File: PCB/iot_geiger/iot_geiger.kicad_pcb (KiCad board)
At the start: 2 copper layers, 99.1 x 63.5 mm, 59 parts, among them J1 Program, J2 Display, J3 IO, J4 5V DC, J5 PM, Q1 BUK7M6R3, Q2 BC817, SW1 SW_Update, U1 NINA-W102, U2 AM2302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

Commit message: fix spiffs
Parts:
- added R19: 10K, Resistor_SMD:R_0603_1608Metric_Pad0.98x0.95mm_HandSolder, F.Cu at (138.7, 79.5)
- added V1: J305, nina:Geiger, F.Cu at (118.1, 44.5)
- moved R8 0.92 mm to (197.4, 68.3)
- moved R4 0.25 mm to (192.8, 81.8)
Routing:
- net +3V3: track 214.1 -> 201.4 mm
- net Net-(C7-Pad2): track 3.57 -> 14.9 mm
- net Net-(R14-Pad2): track 0.00 -> 7.20 mm
- net +5V: track 102.5 -> 104.4 mm
- net Net-(Q1-Pad4): track 2.04 -> 3.82 mm
- net /PM_TxD: track 89.4 -> 87.9 mm
- net GND: track 88.7 -> 90.2 mm, vias 43 -> 45
- net /G_ANA: track 55.9 -> 54.4 mm
- net /PRG_RxD: track 113.8 -> 112.7 mm
- net Net-(R8-Pad1): track 5.69 -> 4.57 mm
- net /PM_RxD: track 85.5 -> 84.7 mm
- net /IO2: track 75.6 -> 74.8 mm
- net /PRG_TxD: track 107.2 -> 106.5 mm
- net /PM_RST: track 78.2 -> 77.6 mm
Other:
- board size 99.1 x 63.5 mm -> 99.1 x 64.5 mm

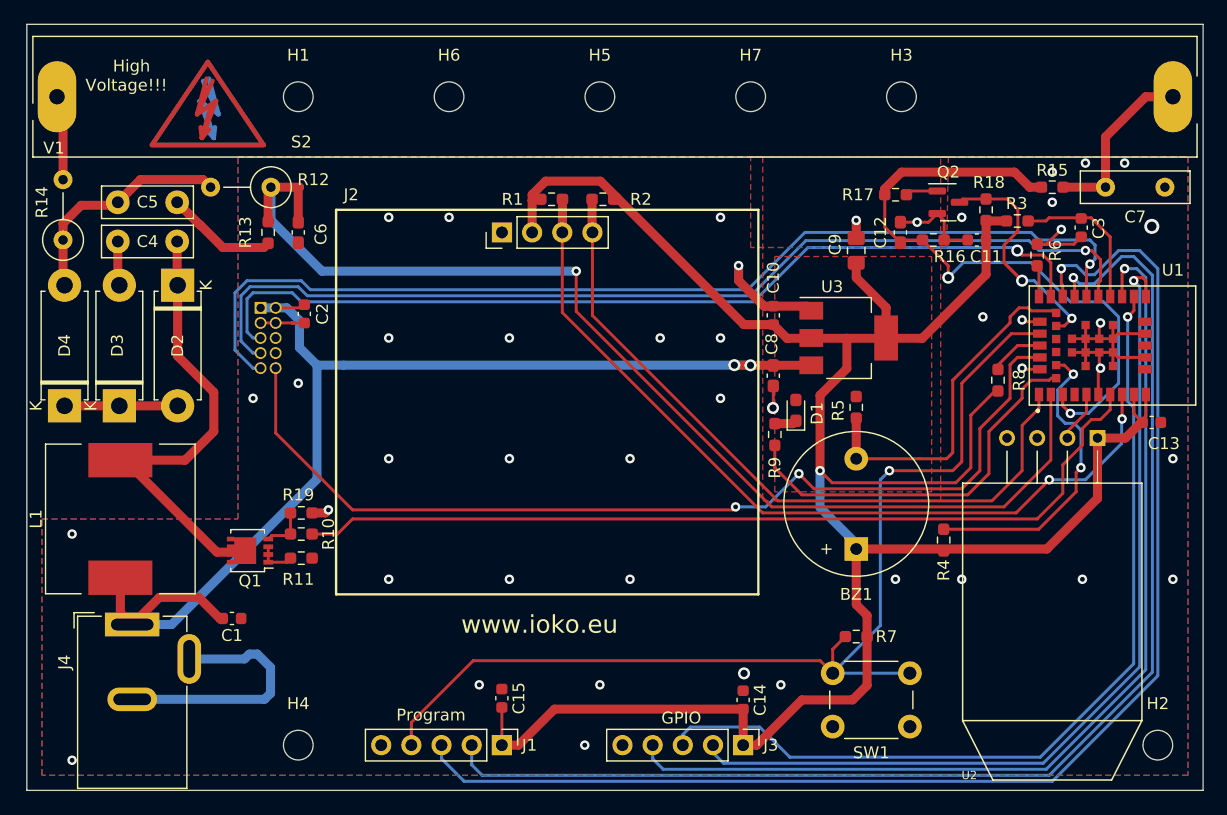
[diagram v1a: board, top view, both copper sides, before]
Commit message: Add PM sensor support
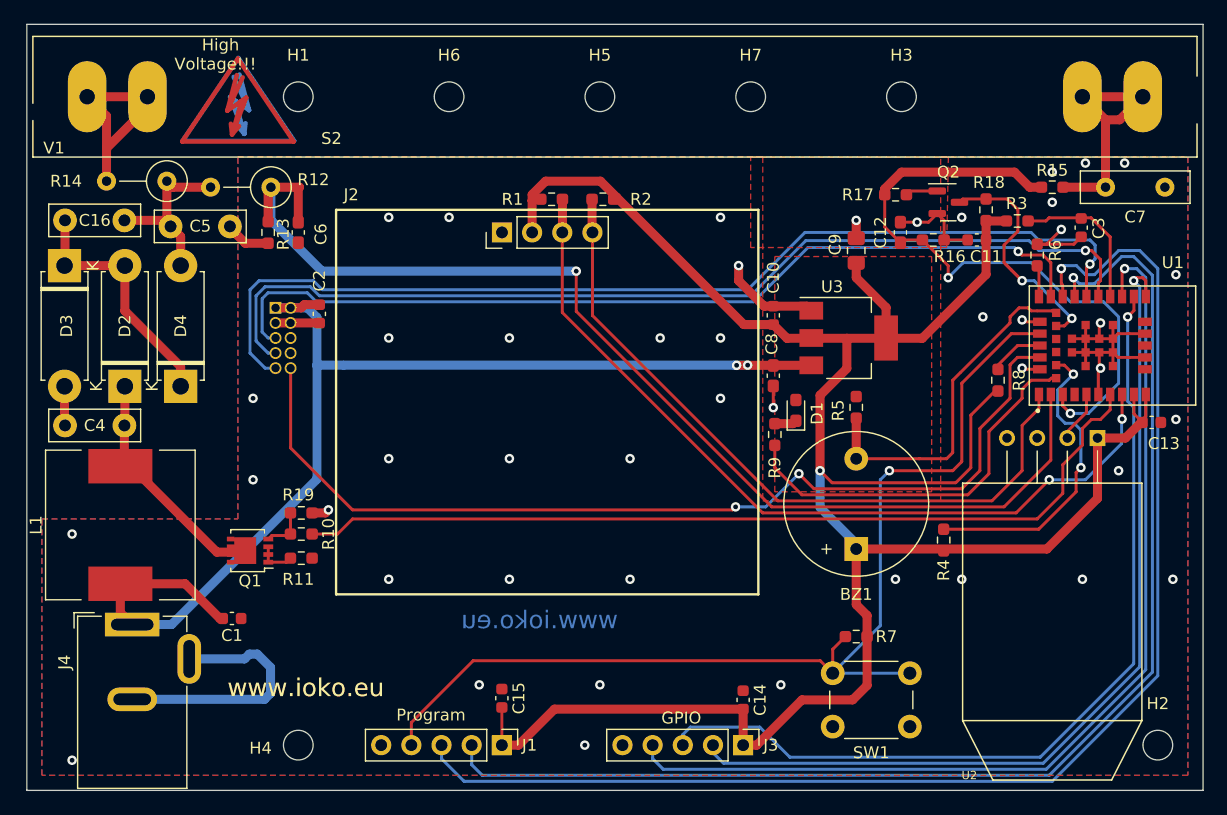
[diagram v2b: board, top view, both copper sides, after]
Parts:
- added C16: 10nF/1000v, Capacitor_THT:C_Disc_D7.5mm_W2.5mm_P5.00mm, F.Cu at (118.8, 54.9)
- C6: value 0.1nF -> 100pF
- R11: value 10R -> 47R
- moved C4 16.1 mm to (123.8, 72.1)
- moved D3 12.7 mm to (118.7, 58.7), turned to -90 degrees
- moved R14 10.0 mm to (127.4, 51.6), turned to 180 degrees
- moved D4 9.92 mm to (128.5, 68.8)
- moved D2 9.60 mm to (123.8, 68.8), turned to 90 degrees
- moved C5 4.89 mm to (132.7, 55.4)
- moved S1 2.60 mm to (133.4, 45.4)
- moved S2 2.56 mm to (133.3, 45.4)
- moved C2 1.27 mm to (140.2, 62.7)
- moved J5 1.26 mm to (136.5, 62.2)
- moved L1 0.51 mm to (123.4, 80.5)
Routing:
- net Net-(C4-Pad1): track 39.9 -> 20.7 mm
- net Net-(D2-Pad2): track 9.53 -> 21.0 mm
- net Net-(R14-Pad2): track 7.20 -> 18.6 mm
- net Net-(C7-Pad2): track 14.9 -> 21.0 mm
- net GND: track 90.2 -> 84.7 mm
- net Net-(D4-Pad2): track 19.4 -> 15.6 mm
- net /PM_RST: track 77.6 -> 76.4 mm
- net /PM_RxD: track 84.7 -> 83.4 mm
- net /PM_TxD: track 87.9 -> 86.9 mm
- net /PM_SET: track 82.6 -> 82.1 mm

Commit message: PCB updated
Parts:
- added R20: 22K, Resistor_SMD:R_0603_1608Metric_Pad0.98x0.95mm_HandSolder, F.Cu at (210.1, 73.7)
- C3: value 100nF -> DNU
- D2, D3, D4: footprint Diode_THT:D_5W_P10.16mm_Horizontal -> Diode_THT:D_DO-41_SOD81_P10.16mm_Horizontal
- Q1: value BUK7M6R3 -> BSS123; footprint Package_TO_SOT_SMD:LFPAK33 -> Package_TO_SOT_SMD:SOT-23
- R11: value 47R -> 10R
- R12: value 22M -> 47M
- R13: value 150K -> 330K
- R15: value 22K -> 10K
- R16: value 100K -> 220K
- R3: value 10K* -> DNU
- R4: value 47K -> DNU
- R5: value 10K -> DNU
- R6, R8: value 47K -> 10K
- moved D2 10.2 mm to (123.7, 58.7), turned to -90 degrees
- moved D3 10.2 mm to (118.9, 68.8), turned to 90 degrees
- moved D4 10.2 mm to (128.5, 58.7), turned to -90 degrees
- moved R11 7.27 mm to (135.6, 76.7), turned to -90 degrees
- moved Q1 2.17 mm to (134.6, 80.5)
- moved C2 1.03 mm to (140.5, 63.7)
- moved J5 0.78 mm to (136.5, 63.0)
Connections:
- C16 pad 1: Net-(D2-Pad2) -> Net-(C16-Pad1)
- C16 pad 2: Net-(D4-Pad2) -> Net-(C16-Pad2)
- C5 pad 2: Net-(D4-Pad2) -> Net-(C16-Pad2)
- D2 pad 1: Net-(C4-Pad1) -> Net-(C16-Pad1)
- D2 pad 2: Net-(D2-Pad2) -> Net-(C4-Pad1)
- D3 pad 1: Net-(D2-Pad2) -> Net-(C4-Pad2)
- D3 pad 2: Net-(C4-Pad2) -> Net-(C16-Pad1)
- D4 pad 1: Net-(D2-Pad2) -> Net-(C16-Pad2)
- D4 pad 2: Net-(D4-Pad2) -> Net-(C4-Pad2)
- Q1 pad 1: Net-(Q1-Pad1) -> Net-(R10-Pad1)
- Q1 pad 2: Net-(Q1-Pad1) -> Net-(R11-Pad2)
- Q1 pad 3: Net-(Q1-Pad1) -> Net-(C4-Pad1)
- R10 pad 1: Net-(Q1-Pad4) -> Net-(R10-Pad1)
- R11 pad 2: Net-(Q1-Pad1) -> Net-(R11-Pad2)
- R12 pad 2: Net-(D4-Pad2) -> Net-(C16-Pad2)
- R14 pad 1: Net-(D4-Pad2) -> Net-(C16-Pad2)
- R19 pad 2: Net-(Q1-Pad4) -> Net-(R10-Pad1)
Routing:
- net Net-(D2-Pad2): track 21.0 -> 0.00 mm
- net Net-(D4-Pad2): track 15.6 -> 0.00 mm
- net Net-(C16-Pad2): track 0.00 -> 15.6 mm
- net Net-(C4-Pad2): track 3.32 -> 17.3 mm
- net /TEMP_SEN: track 4.33 -> 16.8 mm, vias 0 -> 1
- net Net-(C16-Pad1): track 0.00 -> 8.80 mm
- net +5V: track 104.0 -> 108.4 mm
- net Net-(R10-Pad1): track 0.00 -> 4.25 mm
- net Net-(Q1-Pad4): track 3.82 -> 0.00 mm
- net Net-(Q1-Pad1): track 3.31 -> 0.00 mm
- net /SCL: track 70.2 -> 72.7 mm
- net Net-(R11-Pad2): track 0.00 -> 1.98 mm
- net +3V3: track 201.4 -> 202.7 mm
- net Net-(C4-Pad1): track 20.7 -> 19.5 mm
- net /PM_SET: track 82.1 -> 81.3 mm
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
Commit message: AP added
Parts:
- Q1: value BSS123 -> PBHV8540Z; footprint Package_TO_SOT_SMD:SOT-23 -> Package_TO_SOT_SMD:SOT-223
- R10: value 10R -> 2K2
- R11: value 10R -> 47R
- moved R19 7.89 mm to (138.2, 71.6), turned to -90 degrees
- moved R10 5.62 mm to (140.5, 75.9), turned to -90 degrees
- moved R11 5.47 mm to (133.6, 71.6)
- moved Q1 2.84 mm to (135.9, 78.0), turned to -90 degrees
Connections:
- Q1 pad 2: Net-(R11-Pad2) -> Net-(C4-Pad1)
- Q1 pad 3: Net-(C4-Pad1) -> Net-(R11-Pad2)
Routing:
- net Net-(C4-Pad1): track 19.5 -> 26.9 mm
- net GND: track 84.7 -> 83.3 mm
- net /PM_SET: track 81.3 -> 80.6 mm

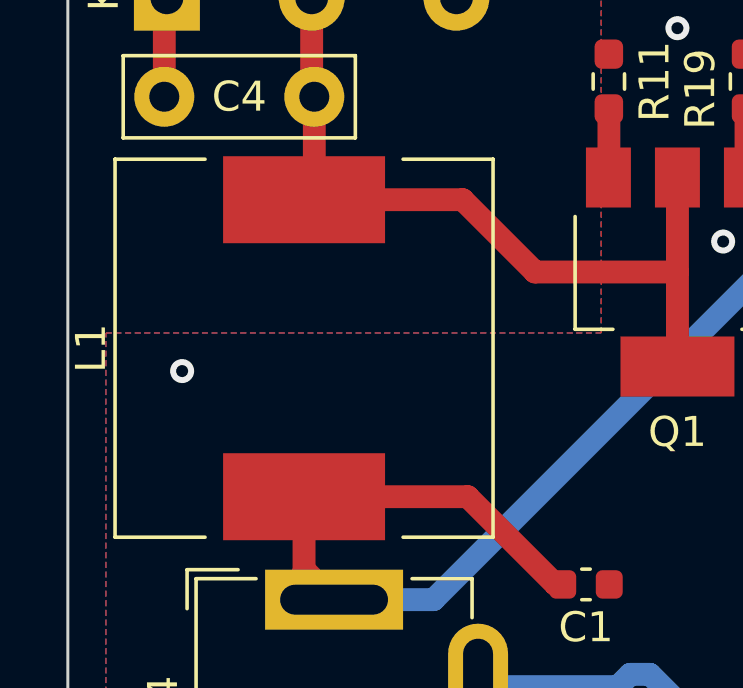
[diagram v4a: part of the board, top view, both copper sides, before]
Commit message: add webserver
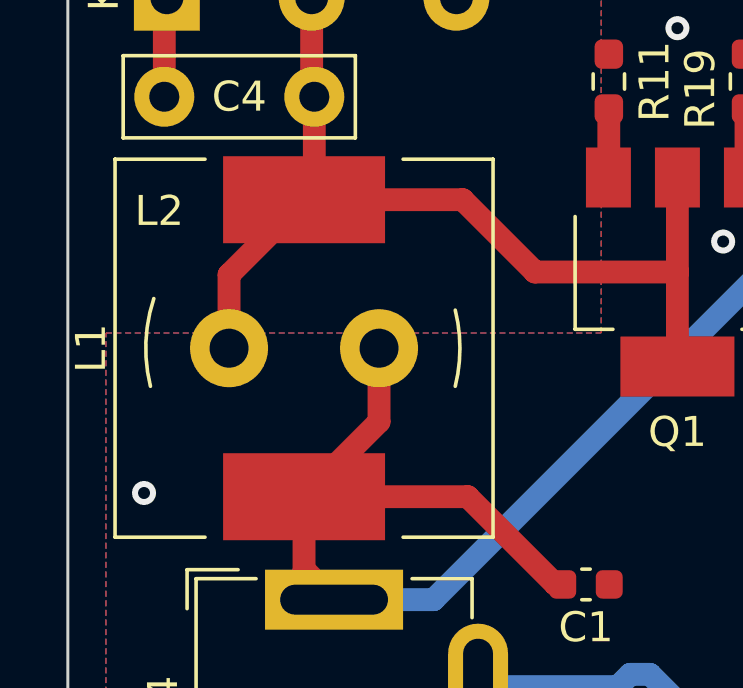
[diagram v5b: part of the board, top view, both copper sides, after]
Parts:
- added L2: DNU, Inductor_THT:L_Radial_D10.0mm_P5.00mm_Fastron_07M, F.Cu at (125.9, 80.5)
- Q1: value PBHV8540Z -> PZTA42
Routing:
- net Net-(C4-Pad1): track 26.9 -> 32.9 mm
- net +5V: track 108.4 -> 114.4 mm
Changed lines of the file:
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@@
   (net 37 "Net-(C16-Pad2)")
   (net 38 "unconnected-(U1-Pad4)")
-  (net 39 "Net-(R10-Pad1)")
-  (net 40 "Net-(R11-Pad2)")
+  (net 39 "Net-(Q1-Pad1)")
+  (net 40 "Net-(Q1-Pad3)")
   (net 41 "Net-(C4-Pad2)")
   (net 42 "Net-(C16-Pad1)")
@@
       (effects (font (size 1 1) (thickness 0.15)))
     )
-    (fp_text value "PBHV8540Z" (at 0 4.5 90) (layer "F.Fab")
+    (fp_text value "PZTA42" (at 0 4.5 90) (layer "F.Fab")
       (effects (font (size 1 1) (thickness 0.15)))
     )
@@
     (fp_line (start -1.85 -2.3) (end -1.85 3.35) (layer "F.Fab") (width 0.1))
     (pad "1" smd rect (at -3.15 -2.3 270) (size 2 1.5) (layers "F.Cu" "F.Paste" "F.Mask")
-      (net 39 "Net-(R10-Pad1)") (pinfunction "B") (pintype "input"))
+      (net 39 "Net-(Q1-Pad1)") (pinfunction "B") (pintype "input"))
     (pad "2" smd rect (at -3.15 0 270) (size 2 1.5) (layers "F.Cu" "F.Paste" "F.Mask")
       (net 32 "Net-(C4-Pad1)") (pinfunction "C") (pintype "passive"))
     (pad "3" smd rect (at -3.15 2.3 270) (size 2 1.5) (layers "F.Cu" "F.Paste" "F.Mask")
-      (net 40 "Net-(R11-Pad2)") (pinfunction "E") (pintype "passive"))
+      (net 40 "Net-(Q1-Pad3)") (pinfunction "E") (pintype "passive"))
     (pad "4" smd rect (at 3.15 0 270) (size 2 3.8) (layers "F.Cu" "F.Paste" "F.Mask")
       (net 32 "Net-(C4-Pad1)") (pinfunction "C") (pintype "passive"))
@@
       (net 6 "GND") (pintype "passive"))
     (pad "2" smd roundrect (at 0.9125 0 270) (size 0.975 0.95) (layers "F.Cu" "F.Paste" "F.Mask") (roundrect_rratio 0.25)
-      (net 39 "Net-(R10-Pad1)") (pintype "passive"))
+      (net 39 "Net-(Q1-Pad1)") (pintype "passive"))
     (model "${KICAD6_3DMODEL_DIR}/Resistor_SMD.3dshapes/R_0603_1608Metric.wrl"
       (offset (xyz 0 0 0))
@@
     )
   )
+  (footprint "Inductor_THT:L_Radial_D10.0mm_P5.00mm_Fastron_07M" (layer "F.Cu")
+    (at 125.944 80.518 180)
+    (descr "Inductor, Radial series, Radial, pin pitch=5.00mm, , diameter=10mm, Fastron, 07M, http://www.fastrongroup.com/image-show/37/07M.pdf?type=Complete-DataSheet&productType=series")
+    (tags "Inductor Radial series Radial pin pitch 5.00mm  diameter 10mm Fastron 07M")
+    (property "Sheetfile" "iot_geiger.kicad_sch")
+    (property "Sheetname" "")
+    (attr through_hole)
+    (fp_text reference "L2" (at 7.326 4.572) (layer "F.SilkS")
+      (effects (font (size 1 1) (thickness 0.15)))
+    )
+    (fp_text value "DNU" (at 2.5 6.25) (layer "F.Fab")
+      (effects (font (size 1 1) (thickness 0.15)))
+    )
+    (fp_text user "${REFERENCE}" (at 2.5 0) (layer "F.Fab")
+      (effects (font (size 1 1) (thickness 0.15)))
+    )
+    (fp_arc (start 7.62 -1.27) (mid 7.772487 0.200953) (end 7.507632 1.655877) (layer "F.SilkS") (width 0.12))
+    (fp_arc (start -2.54 1.27) (mid -2.696344 0) (end -2.54 -1.27) (layer "F.SilkS") (width 0.12))
+    (fp_circle (center 2.5 0) (end 7.75 0) (layer "F.CrtYd") (width 0.05) (fill none))
+    (fp_circle (center 2.5 0) (end 7.5 0) (layer "F.Fab") (width 0.1) (fill none))
+    (pad "1" thru_hole circle (at 0 0 180) (size 2.6 2.6) (drill 1.3) (layers *.Cu *.Mask)
+      (net 18 "+5V") (pinfunction "1") (pintype "input"))
+    (pad "2" thru_hole circle (at 5 0 180) (size 2.6 2.6) (drill 1.3) (layers *.Cu *.Mask)
+      (net 32 "Net-(C4-Pad1)") (pinfunction "2") (pintype "input"))
+    (model "${KICAD6_3DMODEL_DIR}/Inductor_THT.3dshapes/L_Radial_D10.0mm_P5.00mm_Fastron_07M.wrl"
+      (offset (xyz 0 0 0))
+      (scale (xyz 1 1 1))
+      (rotate (xyz 0 0 0))
+    )
+  )
   (footprint "Resistor_SMD:R_0603_1608Metric_Pad0.98x0.95mm_HandSolder" (layer "F.Cu")
     (at 140.462 75.946 -90)
@@
     (fp_line (start -0.8 0.4125) (end -0.8 -0.4125) (layer "F.Fab") (width 0.1))
     (pad "1" smd roundrect (at -0.9125 0 270) (size 0.975 0.95) (layers "F.Cu" "F.Paste" "F.Mask") (roundrect_rratio 0.25)
-      (net 39 "Net-(R10-Pad1)") (pintype "passive"))
+      (net 39 "Net-(Q1-Pad1)") (pintype "passive"))
     (pad "2" smd roundrect (at 0.9125 0 270) (size 0.975 0.95) (layers "F.Cu" "F.Paste" "F.Mask") (roundrect_rratio 0.25)
       (net 22 "/PWM") (pintype "passive"))
@@
       (net 6 "GND") (pintype "passive"))
     (pad "2" smd roundrect (at 0.9125 0 270) (size 0.975 0.95) (layers "F.Cu" "F.Paste" "F.Mask") (roundrect_rratio 0.25)
-      (net 40 "Net-(R11-Pad2)") (pintype "passive"))
+      (net 40 "Net-(Q1-Pad3)") (pintype "passive"))
     (model "${KICAD6_3DMODEL_DIR}/Resistor_SMD.3dshapes/R_0603_1608Metric.wrl"
       (offset (xyz 0 0 0))
@@
   (via (at 201.93 50.8) (size 0.8) (drill 0.4) (layers "F.Cu" "B.Cu") (free) (net 6))
   (via (at 146.05 85.09) (size 0.8) (drill 0.4) (layers "F.Cu" "B.Cu") (free) (net 6))
-  (via (at 119.38 81.28) (size 0.8) (drill 0.4) (layers "F.Cu" "B.Cu") (free) (net 6))
+  (via (at 118.11 85.344) (size 0.8) (drill 0.4) (layers "F.Cu" "B.Cu") (free) (net 6))
   (via (at 166.37 74.93) (size 0.8) (drill 0.4) (layers "F.Cu" "B.Cu") (free) (net 6))
   (via (at 212.344 59.436) (size 0.8) (drill 0.4) (layers "F.Cu" "B.Cu") (free) (net 6))
@@
   (segment (start 181.635 67.07) (end 175.3476 67.07) (width 0.762) (layer "F.Cu") (net 18))
   (segment (start 128.902 85.468) (end 123.444 85.468) (width 0.762) (layer "F.Cu") (net 18))
+  (segment (start 125.944 80.518) (end 125.944 82.968) (width 0.762) (layer "F.Cu") (net 18))
   (segment (start 136.556 62.966) (end 136.515 63.007) (width 0.762) (layer "F.Cu") (net 18))
+  (segment (start 125.944 82.968) (end 123.444 85.468) (width 0.762) (layer "F.Cu") (net 18))
   (segment (start 181.635 67.07) (end 176.516 67.07) (width 0.25) (layer "F.Cu") (net 18))
   (segment (start 176.516 67.07) (end 176.29 67.07) (width 0.25) (layer "F.Cu") (net 18))
@@
   (segment (start 135.89 77.978) (end 131.1425 77.978) (width 0.762) (layer "F.Cu") (net 32))
   (segment (start 123.444 75.568) (end 128.7325 75.568) (width 0.762) (layer "F.Cu") (net 32))
+  (segment (start 120.944 80.518) (end 120.944 78.068) (width 0.762) (layer "F.Cu") (net 32))
   (segment (start 123.785 75.227) (end 123.444 75.568) (width 0.762) (layer "F.Cu") (net 32))
   (segment (start 123.444 75.06) (end 123.828 75.06) (width 0.762) (layer "F.Cu") (net 32))
+  (segment (start 120.944 78.068) (end 123.444 75.568) (width 0.762) (layer "F.Cu") (net 32))
   (segment (start 204.47 44.45) (end 209.55 44.45) (width 0.762) (layer "F.Cu") (net 33))
   (segment (start 207.605 46.395) (end 209.55 44.45) (width 0.762) (layer "F.Cu") (net 33))
